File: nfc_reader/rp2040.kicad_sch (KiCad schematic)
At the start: 31 parts, among them J1 USB_C, J2 Qwiic, J3 DEBUG, SW6 RESET, SW7 BOOT, U4 W25QXX128MBIT, U5 RP2040, Y1 12MHz

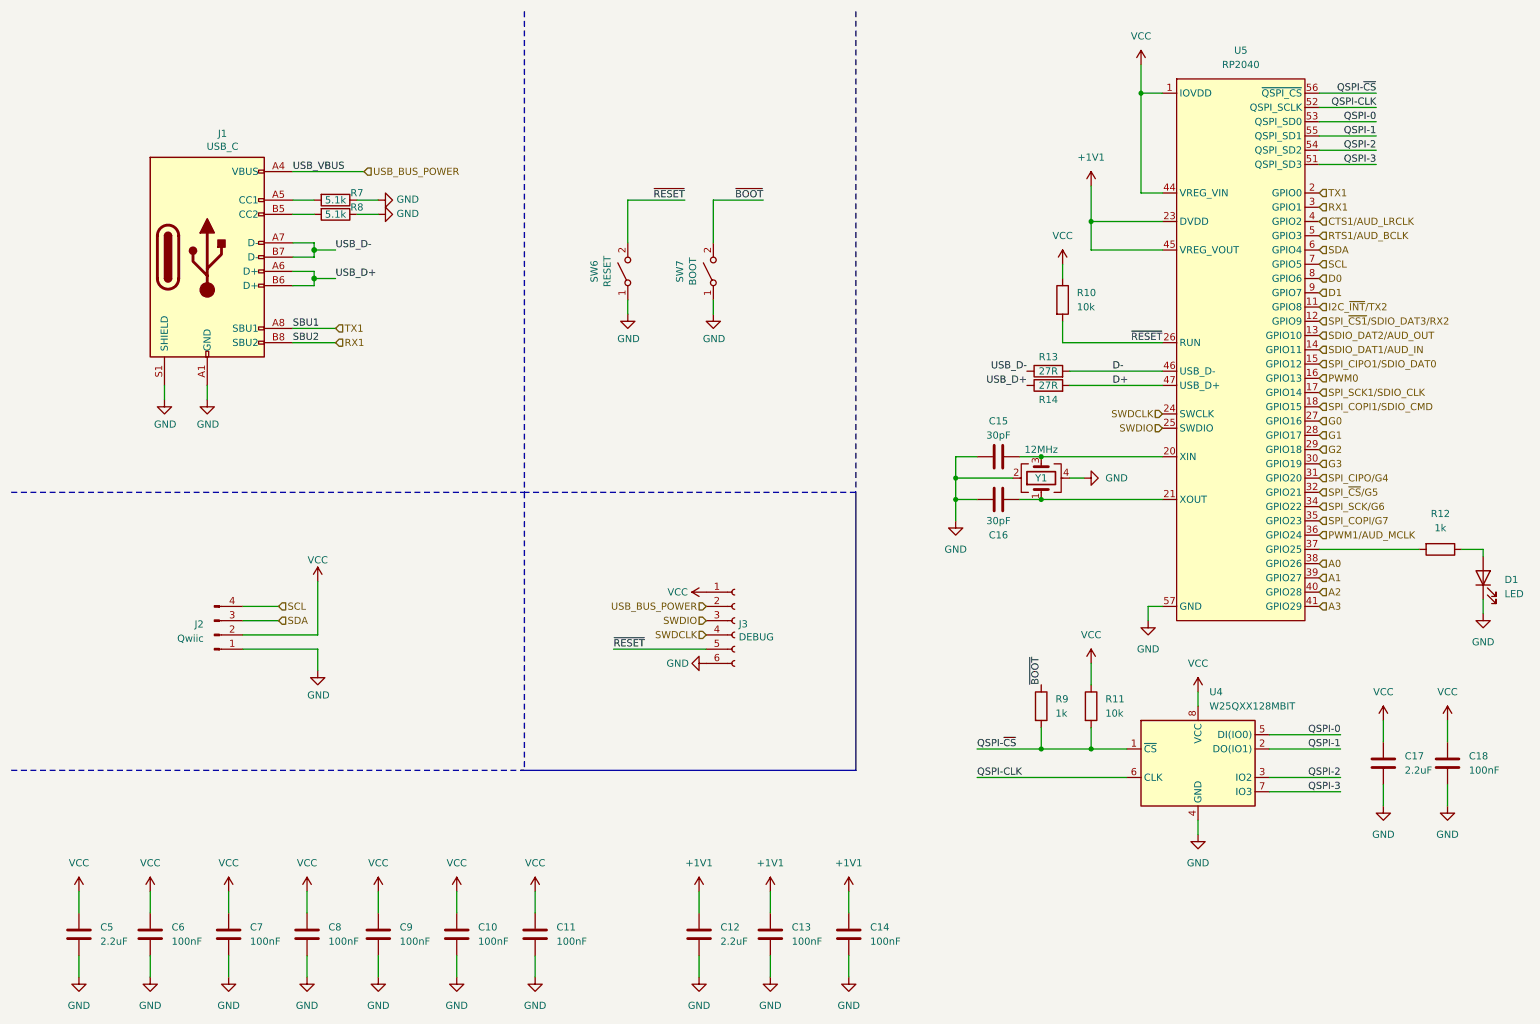
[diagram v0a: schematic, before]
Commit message: Added front artwork to nfc_reader
Also
- Fixed error with missing power to PN7150 radio
- Added two buttons and two LEDs
- Moved things around a little
- Updated BOM and created pos file
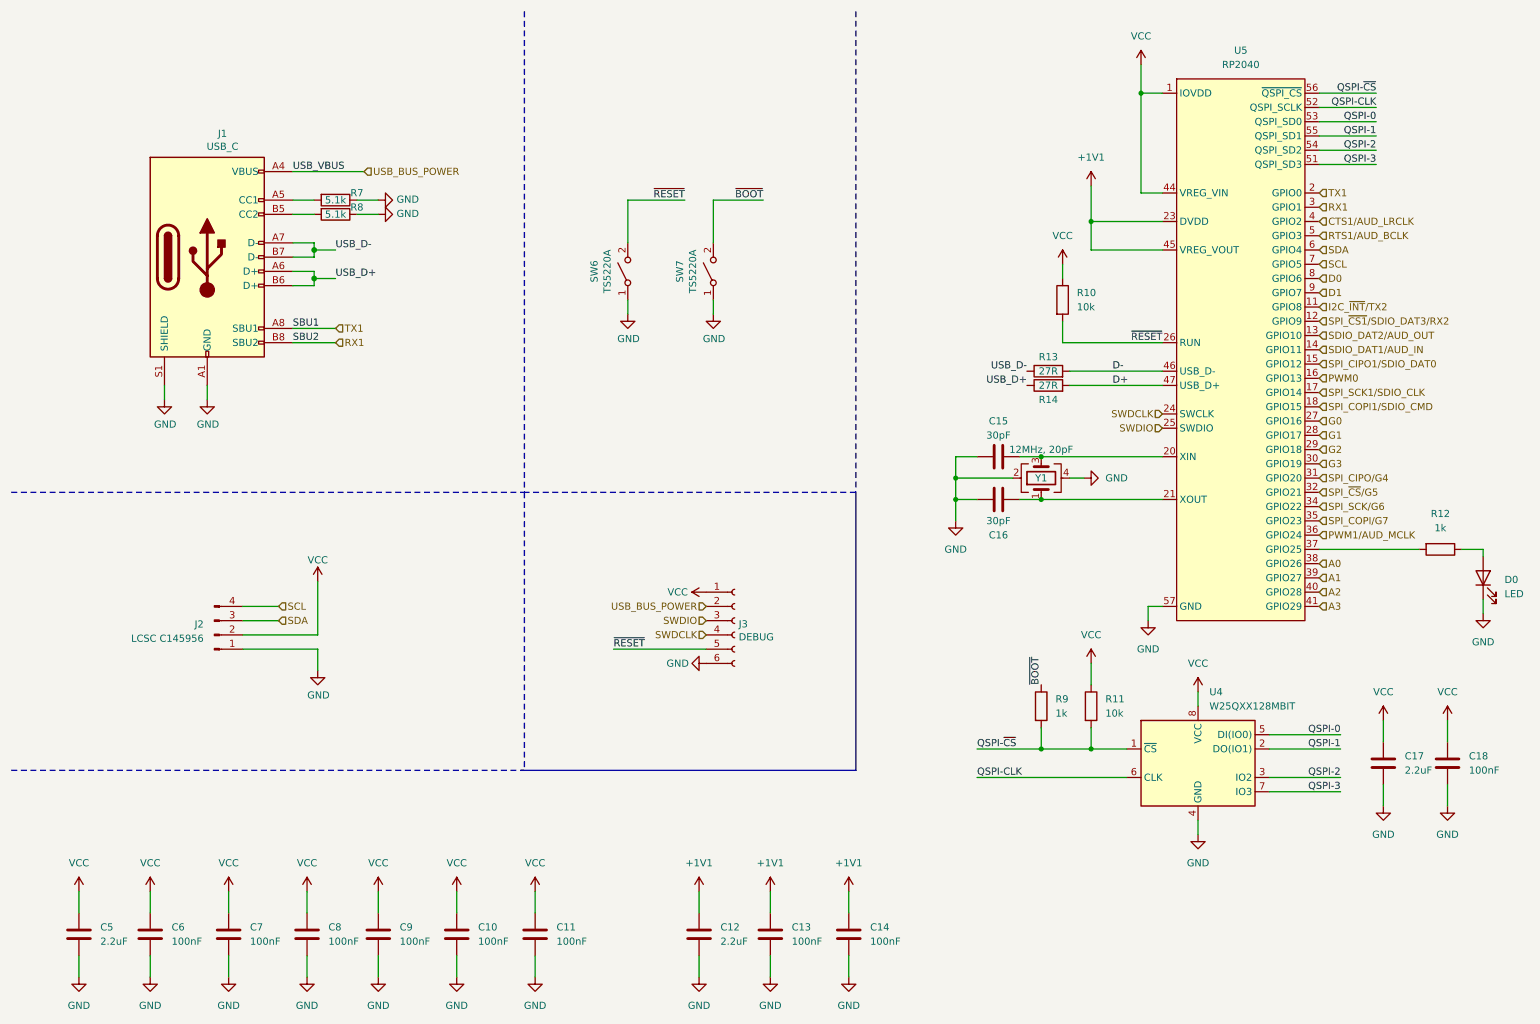
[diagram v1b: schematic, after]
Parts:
- J2: value Qwiic -> LCSC C145956
- J3: now left out of the parts list
- SW6: value RESET -> TS5220A
- SW7: value BOOT -> TS5220A
- Y1: value 12MHz -> 12MHz, 20pF
- renumbered D1 to D0
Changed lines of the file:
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@@
   (title_block
     (title "RP2040 base circuit")
-    (date "2022-06-12")
-    (rev "1.0")
+    (date "2023-06-04")
+    (rev "1.1")
     (comment 1 "CC-BY-SA")
   )
@@
       (effects (font (size 1.27 1.27)))
     )
-    (property "Value" "RESET" (at 118.2624 58.42 0)
+    (property "Value" "TS5220A" (at 118.2624 58.42 0)
       (effects (font (size 1.27 1.27)))
     )
@@
       (effects (font (size 1.27 1.27)))
     )
-    (property "Value" "BOOT" (at 133.5024 58.42 0)
+    (property "Value" "TS5220A" (at 133.5024 58.42 0)
       (effects (font (size 1.27 1.27)))
     )
@@
       (effects (font (size 1.27 1.27)) (justify right))
     )
-    (property "Value" "Qwiic" (at 46.355 123.8249 0)
+    (property "Value" "LCSC C145956" (at 46.355 123.8249 0)
       (effects (font (size 1.27 1.27)) (justify right))
     )
@@
       (effects (font (size 1.27 1.27)))
     )
-    (property "Value" "12MHz" (at 195.58 90.17 90)
+    (property "Value" "12MHz, 20pF" (at 195.58 90.17 90)
       (effects (font (size 1.27 1.27)))
     )
@@
   )
   (symbol (lib_id "Connector:Conn_01x06_Female") (at 140.97 120.65 0) (unit 1)
-    (in_bom yes) (on_board yes) (dnp no)
+    (in_bom no) (on_board yes) (dnp no)
     (property "Reference" "J3" (at 141.6812 121.2596 0)
       (effects (font (size 1.27 1.27)) (justify left))
@@
   (symbol (lib_id "Device:LED") (at 274.32 113.03 90) (unit 1)
     (in_bom yes) (on_board yes) (dnp no) (fields_autoplaced)
-    (property "Reference" "D1" (at 278.13 113.3474 90)
+    (property "Reference" "D0" (at 278.13 113.3474 90)
       (effects (font (size 1.27 1.27)) (justify right))
     )
@@
       (project "nfc_reader"
         (path "/01149b17-33ef-4823-97dd-2a81938478fb/559cdf0d-169d-4cf2-8158-228eb70a146b"
-          (reference "D1") (unit 1)
-        )
-      )
+          (reference "D0") (unit 1)
+        )
+      )
